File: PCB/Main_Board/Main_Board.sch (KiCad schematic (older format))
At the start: 15 parts, among them J1 USB_B_Micro, SW1 SW_DPDT_x2, U1 TLV75533PDBV, U2 ESP32-WROOM-32

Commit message: Continue development - Add USB to UART FT232R IC
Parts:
- removed SW1: SW_DPDT_x2, symbol Switch:SW_DPDT_x2
- added C10: 4.7uF, symbol Device:C_Small
- added C6, C7: 0.1uF, symbol Device:C_Small
- added C8, C9: 100nF, symbol Device:C_Small
- added D5: TX_LED, symbol Device:LED_Small
- added D6: RX_LED, symbol Device:LED_Small
- added Q1: MBT3904DW1, Package_TO_SOT_SMD:SOT-363_SC-70-6, symbol Transistor_BJT:MBT3904DW1
- added R3, R4: CUR_LIMIT, symbol Device:R_Small
- added R5, R6: 10k, symbol Device:R_Small
- added SW0: SW_SPDT, symbol Switch:SW_SPDT
- added SW1: EN, symbol Switch:SW_Push
- added SW2: BOOT, symbol Switch:SW_Push
- added U3: FT232RL, Package_SO:SSOP-28_5.3x10.2mm_P0.65mm, symbol Interface_USB:FT232RL
- D1: renamed from D?; value LED_Small -> 3V3_LED
- gave numbers to parts that had none: 6
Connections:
- net +3V3: now also C8.2, U3.17 (3V3OUT), U3.19 (~RESET~), U3.4 (VCCIO)
- net +5V: now also C10.1, C9.1, SW0.3 (C), U3.20 (VCC)
- net +BATT: now also SW0.1 (A)
- net Earth: now also C10.2, C6.2, C7.2, C8.1, C9.2, R3.2, R4.2, SW1.2, SW2.2, U3.18 (GND), U3.21 (GND), U3.25 (AGND), U3.26 (TEST), U3.7 (GND)
- net IO0: now reaches U2.25 (IO0)
- net IO0: now also C7.1, Q1.3 (C2), SW2.1
- net EN: now reaches C5.2, R1.2, U2.3 (EN)
- net EN: now also C6.1, Q1.6 (C1), SW1.1
- net RXD0: now reaches U2.34 (RXD0/IO3)
- net RXD0: now also U3.1 (TXD)
- net TXD0: now reaches U2.35 (TXD0/IO1)
- net TXD0: now also U3.5 (RXD)
- net at C1.1, U1.1 (IN), U1.3 (EN): now also SW0.2 (B)
- net D-: now reaches D2.1 (A1), J1.2 (D-)
- net D-: now also U3.16 (USBD-)
- net D+: now reaches D3.1 (A1), J1.3 (D+)
- net D+: now also U3.15 (USBD+)
- new net: D6.2 (A), U3.22 (CBUS1)
- new net: D5.2 (A), U3.23 (CBUS0)
- new net: D5.1 (K), R3.1
- new net: D6.1 (K), R4.1
- new net: Q1.2 (B1), R5.1
- new net: Q1.5 (B2), R6.1
- new net ~DTR: Q1.4 (E2), R5.2, U3.2 (~DTR)
- new net ~RTS: Q1.1 (E1), R6.2, U3.3 (~RTS)
- no-connect marks 1 -> 16
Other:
- note added: "~DTR~ ~RTS~ EN IO0\n1 1 1 1\n0 0 1 1\n1 0 0 1\n0 1 1 0"
- moved on the sheet: C5, R1

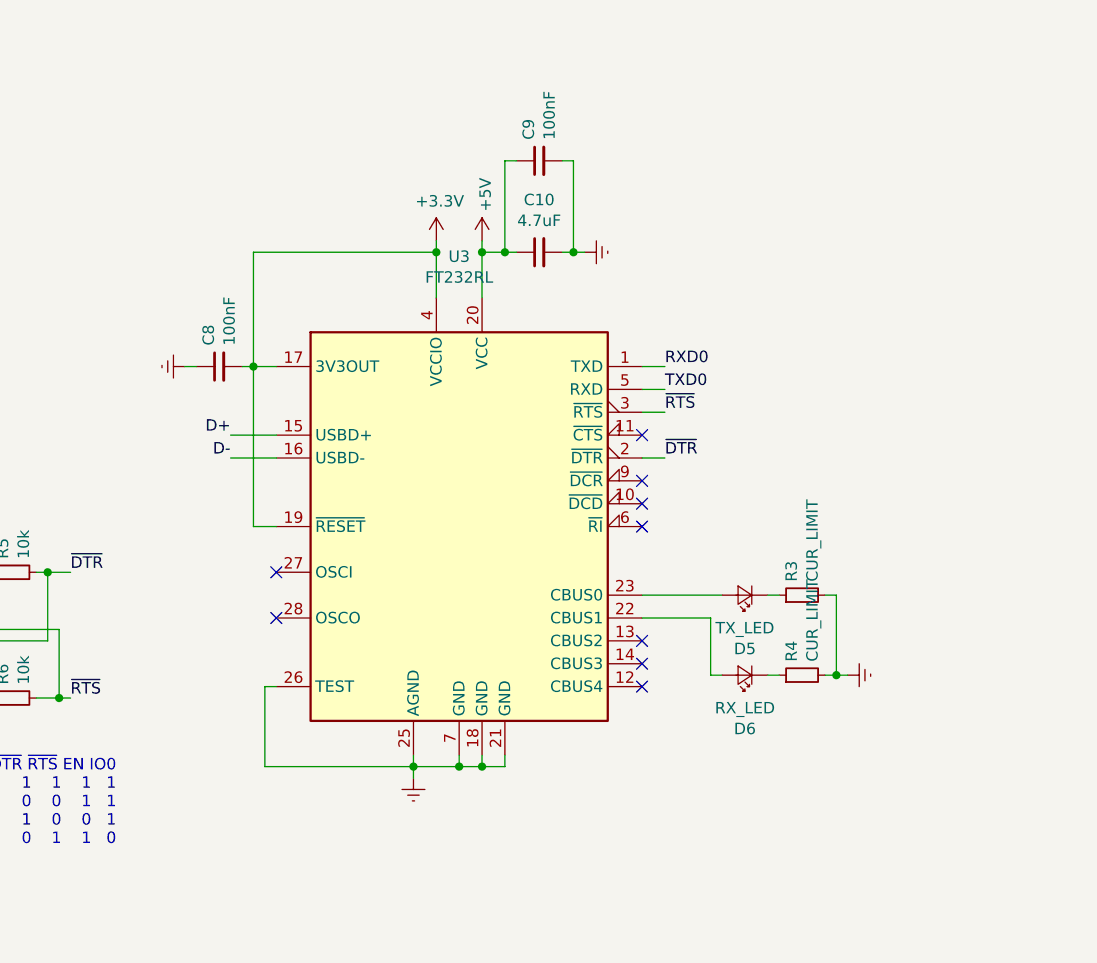
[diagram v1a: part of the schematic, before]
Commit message: Swap USB to UART chip to FT231x to save money and reduce size
FT230x was trialled, but the ESP32 uses the DTR pin RS232 pin to
auto-reset
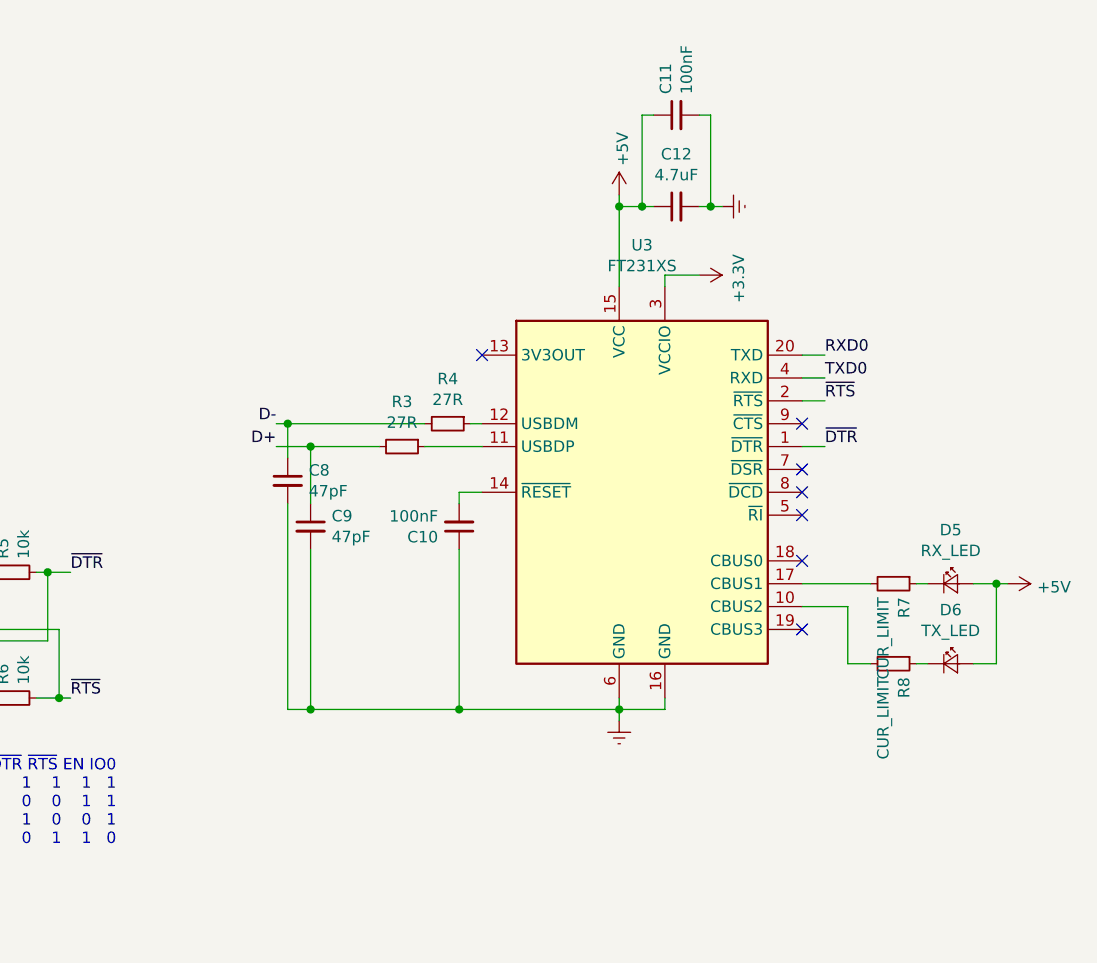
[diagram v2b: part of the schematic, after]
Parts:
- removed U3: FT232RL, Package_SO:SSOP-28_5.3x10.2mm_P0.65mm, symbol Interface_USB:FT232RL
- added C11: 100nF, symbol Device:C_Small
- added C12: 4.7uF, symbol Device:C_Small
- added R7, R8: CUR_LIMIT, symbol Device:R_Small
- added U3: FT231XS, Package_SO:SSOP-20_3.9x8.7mm_P0.635mm, symbol Interface_USB:FT231XS
- C10: value 4.7uF -> 100nF
- C8, C9: value 100nF -> 47pF
- D5: value TX_LED -> RX_LED
- D6: value RX_LED -> TX_LED
- R3, R4: value CUR_LIMIT -> 27R
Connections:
- net +3V3: now also U3.3 (VCCIO); no longer C8.2
- net +5V: now also D5.2 (A), D6.2 (A), C11.1, C12.1, U3.15 (VCC); no longer C10.1, C9.1
- net D+: now also C9.1, R3.2
- net D-: now also C8.1, R4.2
- net Earth: now also C10.1, C8.2, C11.2, C12.2, U3.16 (GND), U3.6 (GND); no longer C10.2, C8.1, R3.2, R4.2
- net RXD0: now also U3.20 (TXD)
- net TXD0: now also U3.4 (RXD)
- net ~DTR: now also U3.1 (~DTR)
- net ~RTS: now also U3.2 (~RTS)
- net at R3.1: now also U3.11 (USBDP); no longer D5.1 (K)
- net at R4.1: now also U3.12 (USBDM); no longer D6.1 (K)
- new net: R8.2, U3.10 (CBUS2)
- new net: C10.2, U3.14 (~RESET)
- new net: R7.2, U3.17 (CBUS1)
- new net: D6.1 (K), R8.1
- new net: D5.1 (K), R7.1
- no-connect marks 16 -> 14

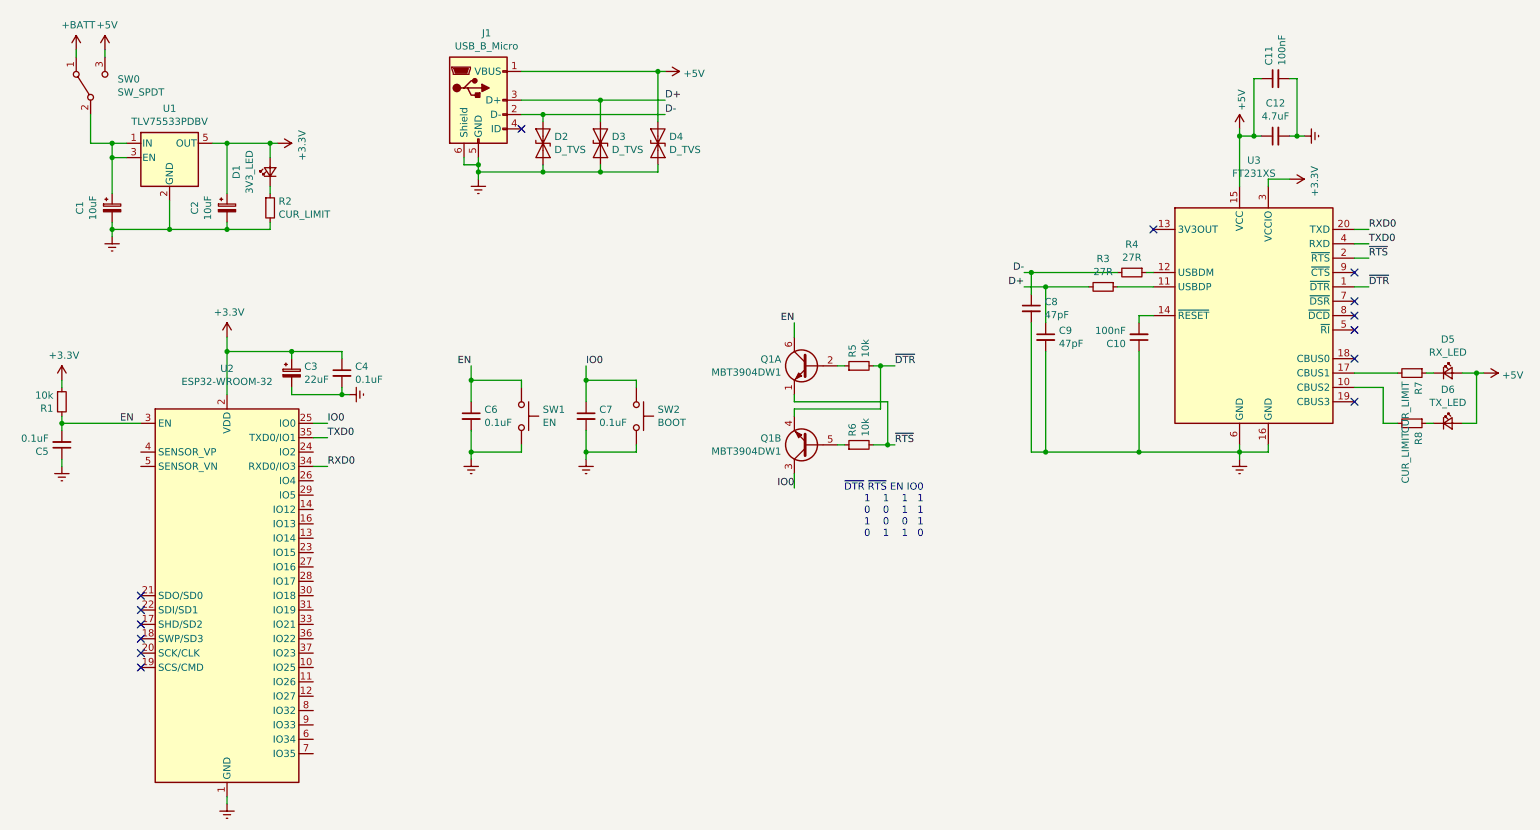
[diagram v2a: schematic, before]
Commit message: Switch to hierarchical sheet system
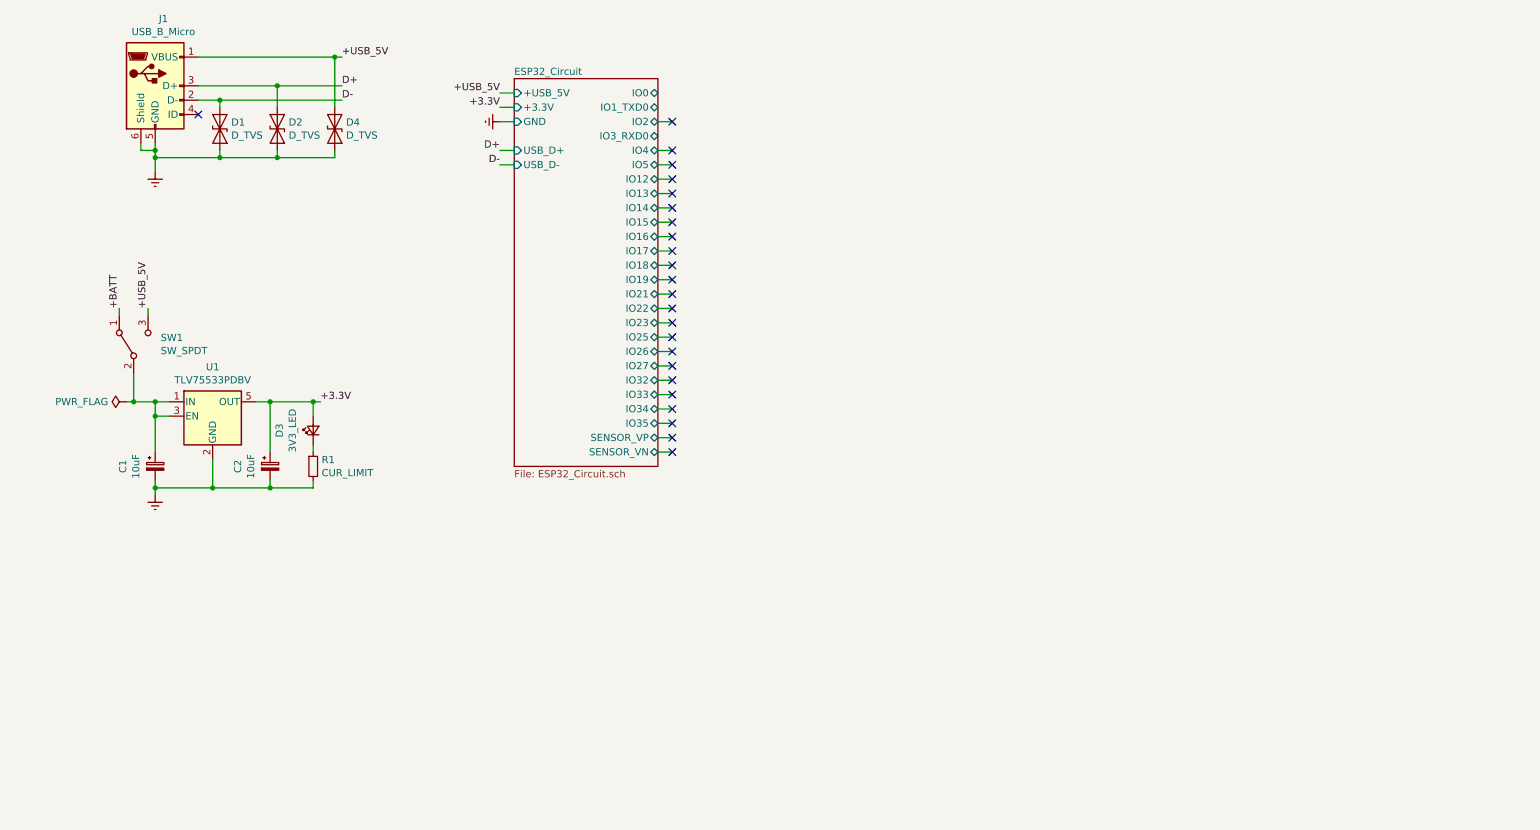
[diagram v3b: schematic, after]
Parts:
- removed C10, C11: 100nF, symbol Device:C_Small
- removed C12: 4.7uF, symbol Device:C_Small
- removed C3: 22uF, symbol Device:CP_Small
- removed C4, C5, C6, C7: 0.1uF, symbol Device:C_Small
- removed C8, C9: 47pF, symbol Device:C_Small
- removed D1: 3V3_LED, symbol Device:LED_Small
- removed D3: D_TVS, symbol Device:D_TVS
- removed D5: RX_LED, symbol Device:LED_Small
- removed D6: TX_LED, symbol Device:LED_Small
- removed Q1: MBT3904DW1, Package_TO_SOT_SMD:SOT-363_SC-70-6, symbol Transistor_BJT:MBT3904DW1
- removed R2, R7, R8: CUR_LIMIT, symbol Device:R_Small
- removed R3, R4: 27R, symbol Device:R_Small
- removed R5, R6: 10k, symbol Device:R_Small
- removed SW0: SW_SPDT, symbol Switch:SW_SPDT
- removed SW1: EN, symbol Switch:SW_Push
- removed SW2: BOOT, symbol Switch:SW_Push
- removed U2: ESP32-WROOM-32, RF_Module:ESP32-WROOM-32, symbol RF_Module:ESP32-WROOM-32
- removed U3: FT231XS, Package_SO:SSOP-20_3.9x8.7mm_P0.635mm, symbol Interface_USB:FT231XS
- added D1: D_TVS, symbol Device:D_TVS
- added D3: 3V3_LED, symbol Device:LED_Small
- added SW1: SW_SPDT, symbol Switch:SW_SPDT
- R1: value 10k -> CUR_LIMIT
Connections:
- net EN is gone; now on net Earth: R1.2
- net +BATT: now also SW1.1 (A)
- net D+: now also D2.1 (A1)
- net D-: now also D1.1 (A1); no longer D2.1 (A1)
- net Earth: now also D1.2 (A2)
- net at C1.1, U1.1 (IN), U1.3 (EN): now also SW1.2 (B)
- net +3V3 renamed +3.3V
- net +3.3V: now also D3.2 (A); no longer R1.1
- net +5V renamed +USB_5V
- net +USB_5V: now also SW1.3 (C)
- new net: D3.1 (K), R1.1
- no-connect marks 14 -> 24
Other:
- note removed: "~DTR~ ~RTS~ EN IO0\n1 1 1 1\n0 0 1 1\n1 0 0 1\n0 1 1 0"
